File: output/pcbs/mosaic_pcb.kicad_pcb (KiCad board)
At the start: 2 copper layers, 100 x 85 mm, 23 parts

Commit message: v0.0.1 prototypes
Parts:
- moved TRRS1 3.12 mm to (234.9, 153.0)
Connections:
- ? pad 12: matrix_inner_top -> matrix_index_top
- ? pad 13: matrix_inner_home -> matrix_index_home
- ? pad 14: matrix_inner_bottom -> matrix_index_bottom
- ? pad 15: matrix_index_top -> matrix_inner_bottom
- ? pad 16: matrix_index_home -> matrix_inner_home
- ? pad 17: matrix_index_bottom -> matrix_inner_top
- ? pad 18: thumbfan_far_home -> thumbfan_near_home
- ? pad 20: thumbfan_near_home -> thumbfan_far_home
- ? pad 4: matrix_ring_top -> matrix_ring_bottom
- ? pad 6: matrix_ring_bottom -> matrix_ring_top
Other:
- outline, holes or cut-outs redrawn
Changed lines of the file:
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@@
       (pad 2 thru_hole oval (at 7.62 -7.62 270) (size 2.5 1.5) (drill 1 (offset -0.5 0)) (layers *.Cu *.Mask) (net 3 "matrix_pinky_home"))
       (pad 3 thru_hole oval (at 7.62 -5.08 270) (size 2.5 1.5) (drill 1 (offset -0.5 0)) (layers *.Cu *.Mask) (net 1 "matrix_pinky_bottom"))
-      (pad 4 thru_hole oval (at 7.62 -2.54 270) (size 2.5 1.5) (drill 1 (offset -0.5 0)) (layers *.Cu *.Mask) (net 7 "matrix_ring_top"))
+      (pad 4 thru_hole oval (at 7.62 -2.54 270) (size 2.5 1.5) (drill 1 (offset -0.5 0)) (layers *.Cu *.Mask) (net 5 "matrix_ring_bottom"))
       (pad 5 thru_hole oval (at 7.62 0 270) (size 2.5 1.5) (drill 1 (offset -0.5 0)) (layers *.Cu *.Mask) (net 6 "matrix_ring_home"))
-      (pad 6 thru_hole oval (at 7.62 2.54 270) (size 2.5 1.5) (drill 1 (offset -0.5 0)) (layers *.Cu *.Mask) (net 5 "matrix_ring_bottom"))
+      (pad 6 thru_hole oval (at 7.62 2.54 270) (size 2.5 1.5) (drill 1 (offset -0.5 0)) (layers *.Cu *.Mask) (net 7 "matrix_ring_top"))
       (pad 7 thru_hole oval (at 7.62 5.08 270) (size 2.5 1.5) (drill 1 (offset -0.5 0)) (layers *.Cu *.Mask) (net 10 "matrix_middle_top"))
       (pad 8 thru_hole oval (at 7.62 7.62 270) (size 2.5 1.5) (drill 1 (offset -0.5 0)) (layers *.Cu *.Mask) (net 9 "matrix_middle_home"))
@@
       (pad 10 thru_hole oval (at 5.08 10.16 180) (size 2.5 1.5) (drill 1 (offset -0.5 0)) (layers *.Cu *.Mask) (net 21 "GP9"))
       (pad 11 thru_hole oval (at 2.54 10.16 180) (size 2.5 1.5) (drill 1 (offset -0.5 0)) (layers *.Cu *.Mask) (net 8 "matrix_middle_bottom"))
-      (pad 12 thru_hole oval (at 0 10.16 180) (size 2.5 1.5) (drill 1 (offset -0.5 0)) (layers *.Cu *.Mask) (net 16 "matrix_inner_top"))
-      (pad 13 thru_hole oval (at -2.54 10.16 180) (size 2.5 1.5) (drill 1 (offset -0.5 0)) (layers *.Cu *.Mask) (net 15 "matrix_inner_home"))
-      (pad 14 thru_hole oval (at -5.08 10.16 180) (size 2.5 1.5) (drill 1 (offset -0.5 0)) (layers *.Cu *.Mask) (net 14 "matrix_inner_bottom"))
-      (pad 15 thru_hole oval (at -7.62 10.16 90) (size 2.5 1.5) (drill 1 (offset -0.5 0)) (layers *.Cu *.Mask) (net 13 "matrix_index_top"))
-      (pad 16 thru_hole oval (at -7.62 7.62 90) (size 2.5 1.5) (drill 1 (offset -0.5 0)) (layers *.Cu *.Mask) (net 12 "matrix_index_home"))
-      (pad 17 thru_hole oval (at -7.62 5.08 90) (size 2.5 1.5) (drill 1 (offset -0.5 0)) (layers *.Cu *.Mask) (net 11 "matrix_index_bottom"))
-      (pad 18 thru_hole oval (at -7.62 2.54 90) (size 2.5 1.5) (drill 1 (offset -0.5 0)) (layers *.Cu *.Mask) (net 19 "thumbfan_far_home"))
+      (pad 12 thru_hole oval (at 0 10.16 180) (size 2.5 1.5) (drill 1 (offset -0.5 0)) (layers *.Cu *.Mask) (net 13 "matrix_index_top"))
+      (pad 13 thru_hole oval (at -2.54 10.16 180) (size 2.5 1.5) (drill 1 (offset -0.5 0)) (layers *.Cu *.Mask) (net 12 "matrix_index_home"))
+      (pad 14 thru_hole oval (at -5.08 10.16 180) (size 2.5 1.5) (drill 1 (offset -0.5 0)) (layers *.Cu *.Mask) (net 11 "matrix_index_bottom"))
+      (pad 15 thru_hole oval (at -7.62 10.16 90) (size 2.5 1.5) (drill 1 (offset -0.5 0)) (layers *.Cu *.Mask) (net 14 "matrix_inner_bottom"))
+      (pad 16 thru_hole oval (at -7.62 7.62 90) (size 2.5 1.5) (drill 1 (offset -0.5 0)) (layers *.Cu *.Mask) (net 15 "matrix_inner_home"))
+      (pad 17 thru_hole oval (at -7.62 5.08 90) (size 2.5 1.5) (drill 1 (offset -0.5 0)) (layers *.Cu *.Mask) (net 16 "matrix_inner_top"))
+      (pad 18 thru_hole oval (at -7.62 2.54 90) (size 2.5 1.5) (drill 1 (offset -0.5 0)) (layers *.Cu *.Mask) (net 17 "thumbfan_near_home"))
       (pad 19 thru_hole oval (at -7.62 0 90) (size 2.5 1.5) (drill 1 (offset -0.5 0)) (layers *.Cu *.Mask) (net 18 "thumbfan_home_home"))
-      (pad 20 thru_hole oval (at -7.62 -2.54 90) (size 2.5 1.5) (drill 1 (offset -0.5 0)) (layers *.Cu *.Mask) (net 17 "thumbfan_near_home"))
+      (pad 20 thru_hole oval (at -7.62 -2.54 90) (size 2.5 1.5) (drill 1 (offset -0.5 0)) (layers *.Cu *.Mask) (net 19 "thumbfan_far_home"))
       (pad 21 thru_hole oval (at -7.62 -5.08 90) (size 2.5 1.5) (drill 1 (offset -0.5 0)) (layers *.Cu *.Mask) (net 22 "3V3"))
       (pad 22 thru_hole oval (at -7.62 -7.62 90) (size 2.5 1.5) (drill 1 (offset -0.5 0)) (layers *.Cu *.Mask) (net 2 "GND"))
@@
     )
       (module TRRS-PJ-320A-dual (layer F.Cu)
-      (at 233.1 150.45 270)
+      (at 234.9 153 270)
       (fp_text reference "TRRS1" (at 0 14.2) (layer Dwgs.User) (effects (font (size 1 1) (thickness 0.15))))
       (fp_text value TRRS-PJ-320A-dual (at 0 -5.6) (layer F.Fab) (effects (font (size 1 1) (thickness 0.15))))
@@
             )
             (gr_line (start 135 163.46854837162425) (end 135 96.5) (angle 90) (layer Edge.Cuts) (width 0.15))
-(gr_line (start 138 93.5) (end 222.5306339544118 93.5) (angle 90) (layer Edge.Cuts) (width 0.15))
-(gr_line (start 225.47468413924256 95.92331242255955) (end 234.93405018483085 144.21437031295022) (angle 90) (layer Edge.Cuts) (width 0.15))
-(gr_line (start 234.99 144.79105789039045) (end 234.99 175.5) (angle 90) (layer Edge.Cuts) (width 0.15))
+(gr_line (start 138 93.5) (end 222.50790643613448 93.5) (angle 90) (layer Edge.Cuts) (width 0.15))
+(gr_line (start 225.45702671810642 95.94982790336303) (end 234.93912028197198 146.77726637633646) (angle 90) (layer Edge.Cuts) (width 0.15))
+(gr_line (start 234.99 147.32743847297297) (end 234.99 175.5) (angle 90) (layer Edge.Cuts) (width 0.15))
 (gr_line (start 231.99 178.5) (end 181.39815375600003 178.5) (angle 90) (layer Edge.Cuts) (width 0.15))
 (gr_line (start 180.5966812817448 178.39095860713735) (end 137.19852752574474 166.35950697876157) (angle 90) (layer Edge.Cuts) (width 0.15))
 (gr_arc (start 138 96.5) (end 138 93.5) (angle -90) (layer Edge.Cuts) (width 0.15))
-(gr_arc (start 222.5306339544118 96.5) (end 225.4746841544118 95.9233124) (angle -78.91709404278944) (layer Edge.Cuts) (width 0.15))
-(gr_arc (start 231.99 144.79105789039045) (end 234.99 144.79105789039045) (angle -11.082905957206005) (layer Edge.Cuts) (width 0.15))
+(gr_arc (start 222.50790643613448 96.5) (end 225.45702673613448 95.9498279) (angle -79.43267878539729) (layer Edge.Cuts) (width 0.15))
+(gr_arc (start 231.99 147.32743847297297) (end 234.99 147.32743847297297) (angle -10.567321214594081) (layer Edge.Cuts) (width 0.15))
 (gr_arc (start 231.99 175.5) (end 231.99 178.5) (angle -90) (layer Edge.Cuts) (width 0.15))
 (gr_arc (start 181.39815375600003 175.5) (end 180.59668125600004 178.3909586) (angle -15.495190976470326) (layer Edge.Cuts) (width 0.15))

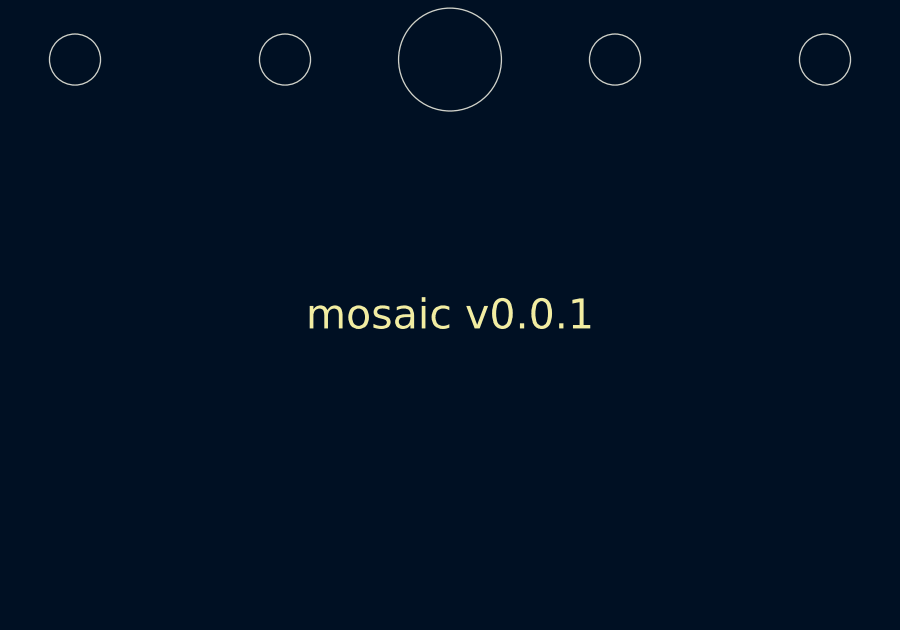
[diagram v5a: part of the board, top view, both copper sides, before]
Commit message: v0.1.0: cleaner routing for split comm traces
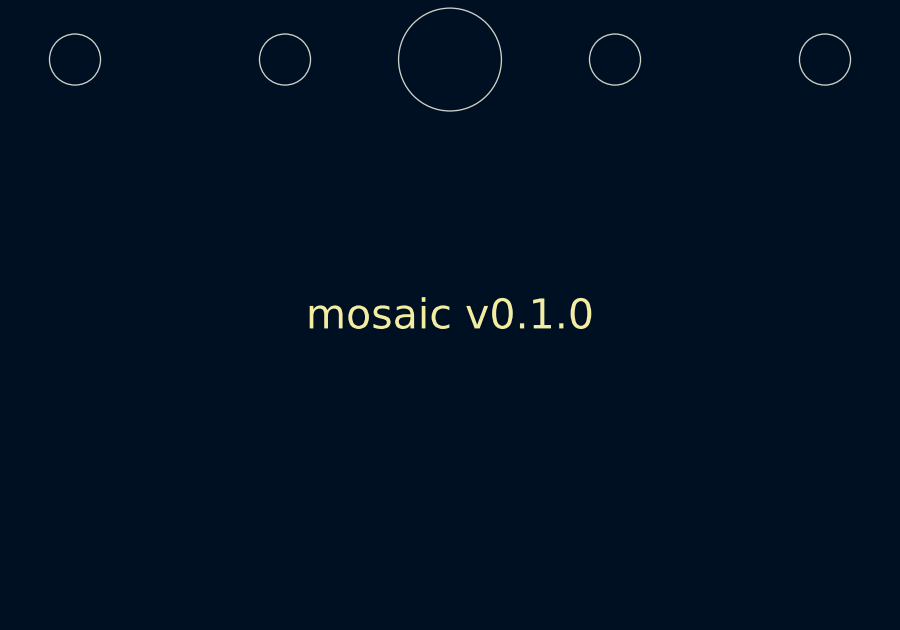
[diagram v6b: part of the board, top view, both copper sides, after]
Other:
- board text added: "mosaic v0.1.0"
- board text removed: "mosaic v0.0.1"
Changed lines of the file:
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@@
                 (effects (font (size 1 1) (thickness 0.15)) )
             )
-            (gr_text "mosaic v0.0.1" (at 198 144.5 0) (layer F.SilkS)
+            (gr_text "mosaic v0.1.0" (at 198 144.5 0) (layer F.SilkS)
                 (effects (font (size 1 1) (thickness 0.15)) )
             )
